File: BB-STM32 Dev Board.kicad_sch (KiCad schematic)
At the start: 58 parts, among them IC1 FT260Q, IC2 TPS63070RNMR, J1 216990-0003, J2 SPI, J3 USART, J4 SWD, J5 I2C, J6 3V-16V, J7 BATTERY, SW1 BOOT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

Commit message: First Run of board.
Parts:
- removed C10: 10uF, Capacitor_SMD:C_0402_1005Metric_Pad0.74x0.62mm_HandSolder, symbol Device:C_Small
- removed C11: 47uF, Capacitor_SMD:C_0402_1005Metric_Pad0.74x0.62mm_HandSolder, symbol Device:C_Small
- removed C9: 100nF, Capacitor_SMD:C_0402_1005Metric_Pad0.74x0.62mm_HandSolder, symbol Device:C_Small
- removed IC2: TPS63070RNMR, Converter_DCDC_Custom:TPS630701RNMR, symbol Regulator_Switching_Custom:TPS63070RNMR
- removed M1: ~, Wireless_Custom:BB-STM32WL, symbol Wireless_Custom:BB-STM32WL
- removed R13: 470K, Resistor_SMD:R_0402_1005Metric_Pad0.72x0.64mm_HandSolder, symbol Device:R_Small_US
- removed R14: 150K, Resistor_SMD:R_0402_1005Metric_Pad0.72x0.64mm_HandSolder, symbol Device:R_Small_US
- added D7, D8: ~, Diode_SMD:D_SOD-123, symbol Diode:1N4148W
- added J8, J9: Conn_01x12, Connector_PinSocket_2.54mm:PinSocket_1x12_P2.54mm_Vertical, symbol Connector_Generic:Conn_01x12
- added R20: 50K, Resistor_SMD:R_0402_1005Metric_Pad0.72x0.64mm_HandSolder, symbol Device:R_Small_US
- added R21: 97K, Resistor_SMD:R_0402_1005Metric_Pad0.72x0.64mm_HandSolder, symbol Device:R_Small_US
- added SW4: ON_OFF, Button_Switch_THT:SW_Slide_SPDT_Angled_CK_OS102011MA1Q, symbol Switch:SW_SPDT
- added U2: TLV62569PDDCR, Component Libraries:SOT95P280X110-6N, symbol TLV62569PDDCR:TLV62569PDDCR
- C1, C3, C5: Manufacturer_Name (none) -> Samsung; Manufacturer_Part_Number (none) -> CL05A475MP5NRNC
- C12, C13, C8: footprint Capacitor_SMD:C_0402_1005Metric_Pad0.74x0.62mm_HandSolder -> Capacitor_SMD:C_0805_2012Metric_Pad1.18x1.45mm_HandSolder
- C2, C4, C6: Manufacturer_Name (none) -> Samsung; Manufacturer_Part_Number (none) -> CL05B104KP5NNNC
- C7: value 22uF -> 4.7uF; Manufacturer_Part_Number CL21A226MAYNNNE -> CL05A475MP5NRNC
- D1, D2, D5, D6: Manufacturer_Name (none) -> Harvatek; Manufacturer_Part_Number (none) -> B1811URO-20D000113U1930
- D4: footprint Diode_SMD:D_SOD-323_HandSoldering -> Diode_SMD:D_SOD-123; Manufacturer_Name EVVO -> Panjit International Inc.; Manufacturer_Part_Number SD103AWS -> SBA140AS_R1_00001
- IC1: footprint FT260Q:QFN50P500X500X80-29N-D -> Component Libraries:QFN50P500X500X80-29N-D
- J1: footprint 216990-0003:2169900003 -> Component Libraries:2169900003
- J2, J3: Manufacturer_Name (none) -> Wurth; Manufacturer_Part_Number (none) -> 61300611821
- J4, TP1: now not fitted
- J5: Manufacturer_Name (none) -> Wurth; Manufacturer_Part_Number (none) -> 61300411821
- J6, J7: Manufacturer_Name (none) -> Molex; Manufacturer_Part_Number (none) -> 0532610271
- L1: value 2.2uH -> 1uH; footprint Inductor_SMD:L_0805_2012Metric_Pad1.15x1.40mm_HandSolder -> Component Libraries:Bourns SRP4020TA; Manufacturer_Name INPAQ -> CoilCraft; Manufacturer_Part_Number WIP201610S-2R2MLDG -> XFL4020-102MEB
- R1, R2, R3: Manufacturer_Name (none) -> Yageo; Manufacturer_Part_Number (none) -> RC0402FR-075K1L
- R10, R9: value ???? -> 665; Manufacturer_Name (none) -> Panasonic; Manufacturer_Part_Number (none) -> ERJ-2RKF6650X
- R11: value 10K -> 453K; Manufacturer_Name Yageo -> Vishay; Manufacturer_Part_Number RC0402JR-0710KL -> CRCW0402453KFKED
- R12: Manufacturer_Name Yageo -> Vishay; Manufacturer_Part_Number RC0402FR-07100KL -> CRCW0402100KFKED
- R16, R17: value ???? -> 665; Manufacturer_Name Yageo -> Panasonic; Manufacturer_Part_Number RC0402JR-0710KL -> ERJ-2RKF6650X
- R18, R19: Manufacturer_Part_Number RC0402JR-0710KL -> RC0402JR-071KL
- R4, R5: Manufacturer_Name (none) -> Yageo; Manufacturer_Part_Number (none) -> RC0402FR-0733RL
- R6, R7, R8: Manufacturer_Name (none) -> Yageo; Manufacturer_Part_Number (none) -> RC0402JR-0710KL
- U1: Manufacturer_Name (none) -> Microchip; Manufacturer_Part_Number (none) -> MCP73831T-2ACI/MC
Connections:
- net +3V3: now also C8.1, L1.2, R11.2, J8.7 (Pin_7); no longer R12.1
- net GND: now also R12.1, J8.8 (Pin_8), J9.6 (Pin_6), R21.1, SW4.1 (A), U2.2 (GND)
- net NRST: now also J8.6 (Pin_6)
- net SWCLK: now also J8.1 (Pin_1)
- net SWDIO: now also J8.2 (Pin_2)
- net USB_CTS: now also J9.4 (Pin_4)
- net USB_RTS: now also J9.5 (Pin_5)
- net USB_RXD: now also J9.7 (Pin_7)
- net USB_TXD: now also J9.8 (Pin_8)
- net USB_VBUS: now also D7.2 (A)
- net VBAT: now also R20.2, SW4.2 (B), U2.1 (EN), U2.4 (VIN); no longer C12.1, C8.1, J7.1 (Pin_1), R11.1, R16.2, U1.3 (V_{BAT}), U1.4 (V_{BAT})
- net at SW1.2: now also J8.10 (Pin_10)
- net at J2.4 (Pin_4): now also J9.9 (Pin_9)
- net at J2.3 (Pin_3): now also J9.10 (Pin_10)
- net at J2.2 (Pin_2): now also J9.11 (Pin_11)
- net at J2.1 (Pin_1): now also J9.12 (Pin_12)
- net at J5.1 (Pin_1): now also J8.3 (Pin_3)
- net at J5.2 (Pin_2): now also J8.4 (Pin_4)
- net at C13.1, D4.1 (K), J6.1 (Pin_1)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: now also D7.1 (K)
- net at L1.1: now also U2.3 (SW)
- net at R12.2: now also R11.1, U2.6 (FB)
- new net: D8.1 (K), J7.1 (Pin_1), SW4.3 (C)
- new net: C12.1, D8.2 (A), R16.2, U1.3 (V_{BAT}), U1.4 (V_{BAT})
- new net: J8.5 (Pin_5), R20.1, R21.2
- no-connect marks 20 -> 22
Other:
- note added: "3V3"
- note added: "CS"
- note added: "CTS"
- note added: "GND"
- note added: "MISO"
- note added: "MOSI"
- note added: "RTS"
- note added: "RXD"
- note added: "SCK"
- note added: "SCL"
- note added: "SDA"
- note added: "TXD"
- moved on the sheet: C12, D3, J5, R15, SW1, SW2

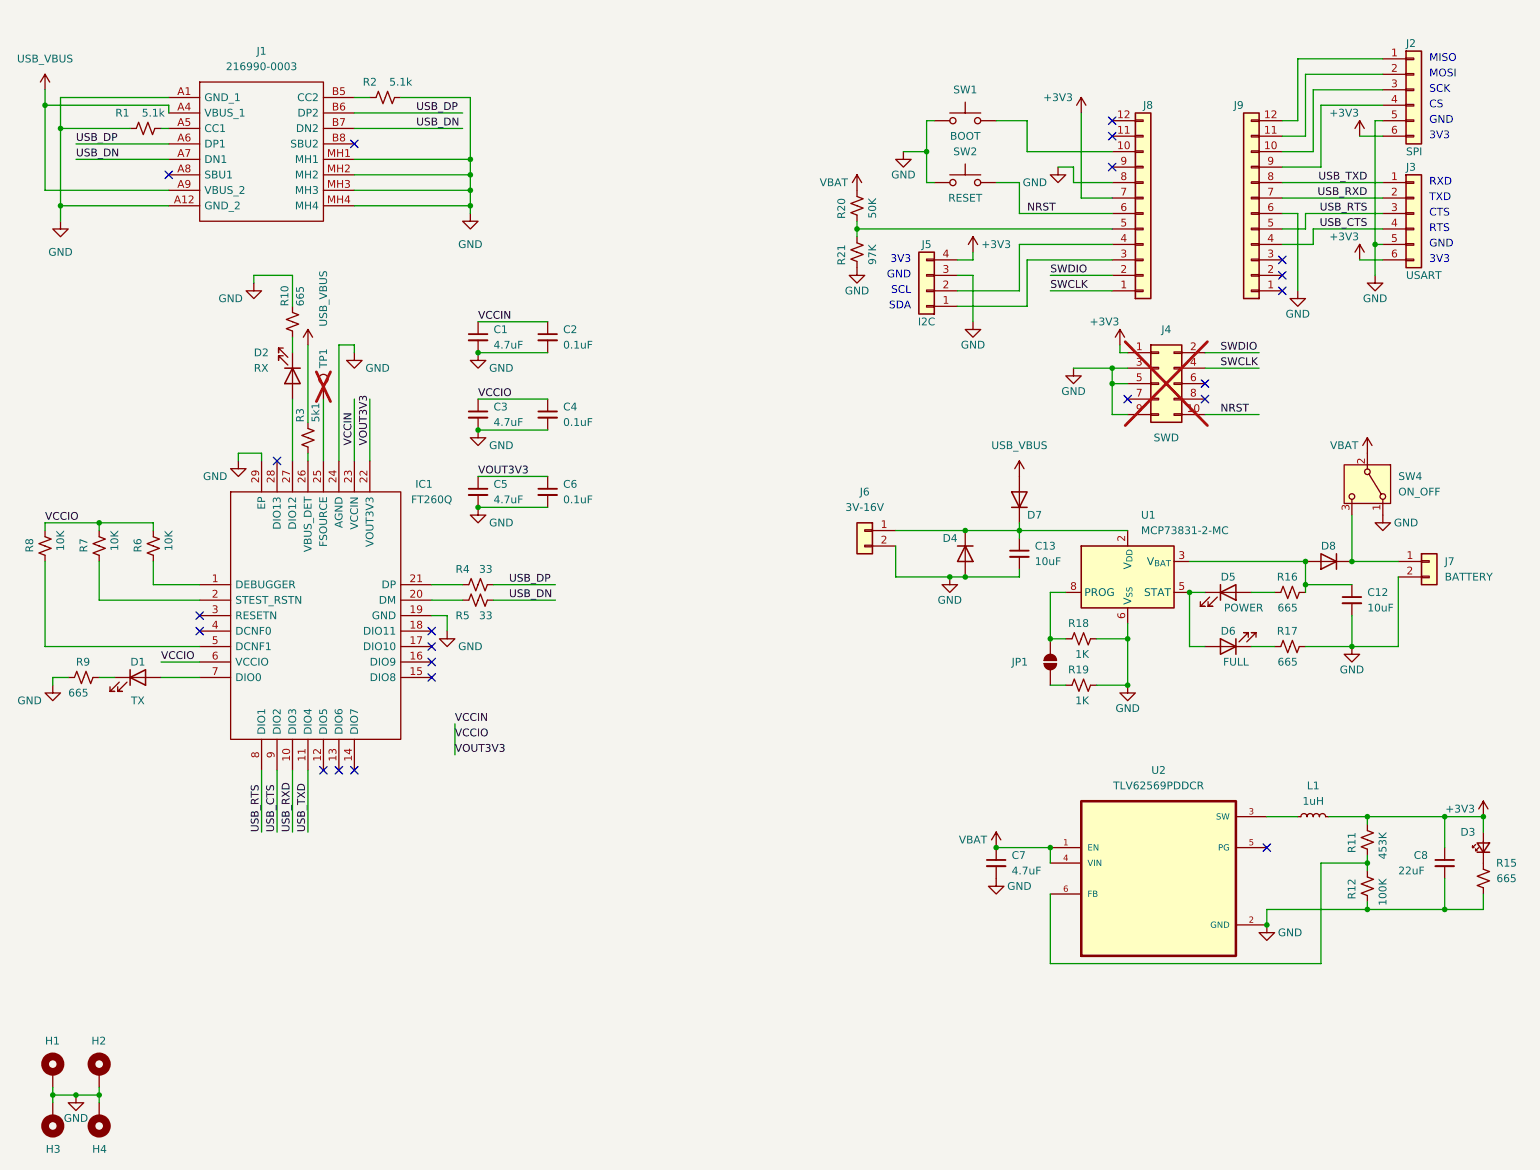
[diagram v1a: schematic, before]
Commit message: Added Images and fixed USB Virtual COM Port.
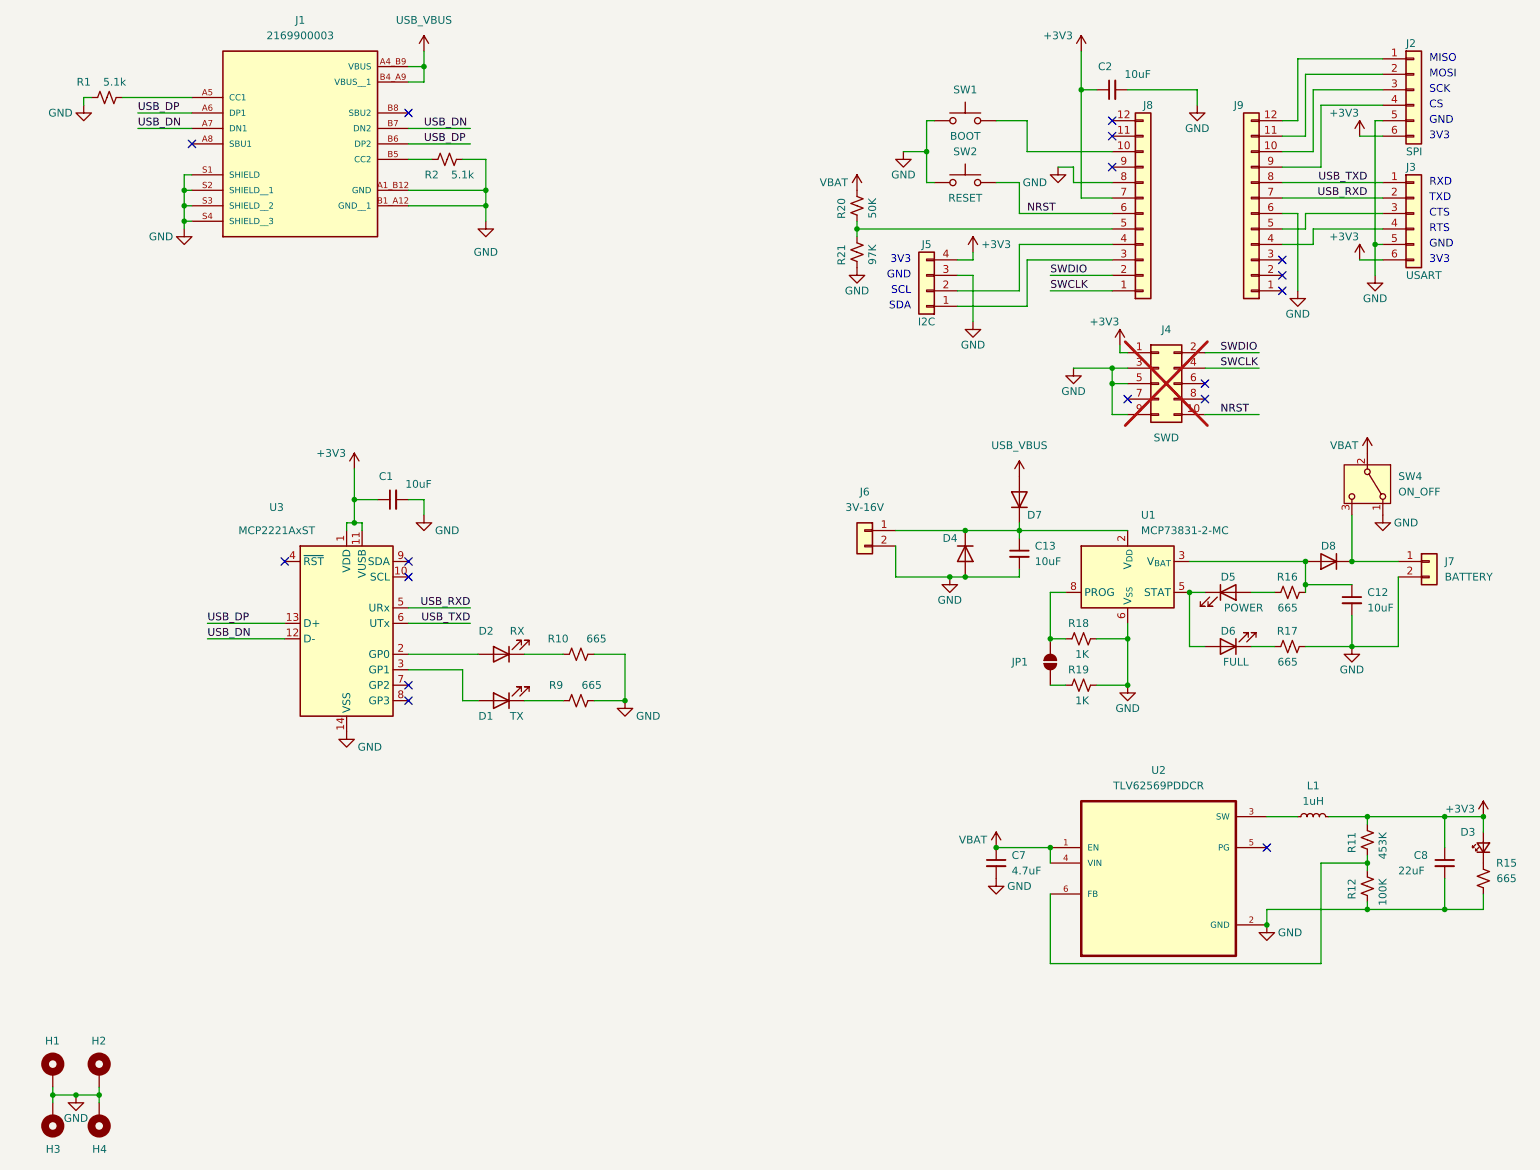
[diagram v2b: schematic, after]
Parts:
- removed C3, C5: 4.7uF, Capacitor_SMD:C_0402_1005Metric_Pad0.74x0.62mm_HandSolder, symbol Device:C_Small
- removed C4, C6: 0.1uF, Capacitor_SMD:C_0402_1005Metric_Pad0.74x0.62mm_HandSolder, symbol Device:C_Small
- removed IC1: FT260Q, Component Libraries:QFN50P500X500X80-29N-D, symbol FT260Q:FT260Q
- removed J1: 216990-0003, Component Libraries:2169900003, symbol 216990-0003:216990-0003
- removed R3: 5k1, Resistor_SMD:R_0402_1005Metric_Pad0.72x0.64mm_HandSolder, symbol Device:R_Small_US
- removed R4, R5: 33, Resistor_SMD:R_0402_1005Metric_Pad0.72x0.64mm_HandSolder, symbol Device:R_Small_US
- removed R6, R7, R8: 10K, Resistor_SMD:R_0402_1005Metric_Pad0.72x0.64mm_HandSolder, symbol Device:R_Small_US
- removed TP1: TestPoint, TestPoint:TestPoint_Loop_D1.80mm_Drill1.0mm_Beaded, symbol Connector:TestPoint
- added J1: 2169900003, Downloaded Footprints:MOLEX_2169900003, symbol 2169900003:2169900003
- added U3: MCP2221AxST, Package_SO:TSSOP-14_4.4x5mm_P0.65mm, symbol Interface_USB:MCP2221AxST
- C1: value 4.7uF -> 10uF; footprint Capacitor_SMD:C_0402_1005Metric_Pad0.74x0.62mm_HandSolder -> Capacitor_SMD:C_0805_2012Metric_Pad1.18x1.45mm_HandSolder; Manufacturer_Part_Number CL05A475MP5NRNC -> CL21A106KOQNNNE
- C2: value 0.1uF -> 10uF; footprint Capacitor_SMD:C_0402_1005Metric_Pad0.74x0.62mm_HandSolder -> Capacitor_SMD:C_0805_2012Metric_Pad1.18x1.45mm_HandSolder; Manufacturer_Part_Number CL05B104KP5NNNC -> CL21A106KOQNNNE
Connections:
- net VCCIN is gone; now on net +3V3: C1.1, C2.1
- net +3V3: now also U3.1 (VDD), U3.11 (VUSB)
- net GND: now also J1.A1_B12 (GND), J1.B1_A12 (GND__1), J1.S1 (SHIELD), J1.S2 (SHIELD__1), J1.S3 (SHIELD__2), J1.S4 (SHIELD__3), U3.14 (VSS)
- net USB_DN: now also J1.A7 (DN1), J1.B7 (DN2), U3.12 (D-)
- net USB_DP: now also J1.A6 (DP1), J1.B6 (DP2), U3.13 (D+)
- net USB_RXD: now also U3.5 (URx)
- net USB_TXD: now also U3.6 (UTx)
- net USB_VBUS: now also J1.A4_B9 (VBUS), J1.B4_A9 (VBUS__1)
- net at R1.2: now also J1.A5 (CC1)
- net at R2.1: now also J1.B5 (CC2)
- net at D2.2 (A): now also U3.2 (GP0)
- net at D1.2 (A): now also U3.3 (GP1)
- net USB_CTS: no longer names the net of J3.4 (Pin_4), J9.4 (Pin_4)
- net USB_RTS: no longer names the net of J3.3 (Pin_3), J9.5 (Pin_5)
- no-connect marks 22 -> 17
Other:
- moved on the sheet: D1, D2, R1, R10, R2, R9
